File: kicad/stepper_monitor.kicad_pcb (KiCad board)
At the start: 2 copper layers, 53 parts, among them J1 USB_C_Receptacle_USB2.0, J2 Conn_01x02_Male, J3 JTAG, J4 Conn_01x04_Male, J5 Conn_01x04_Male, Q1 UMH3N, Q2 PJA3439, Q3 AO3416, SW1 SW_Push, U1 CP2102N-A01-GQFN28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

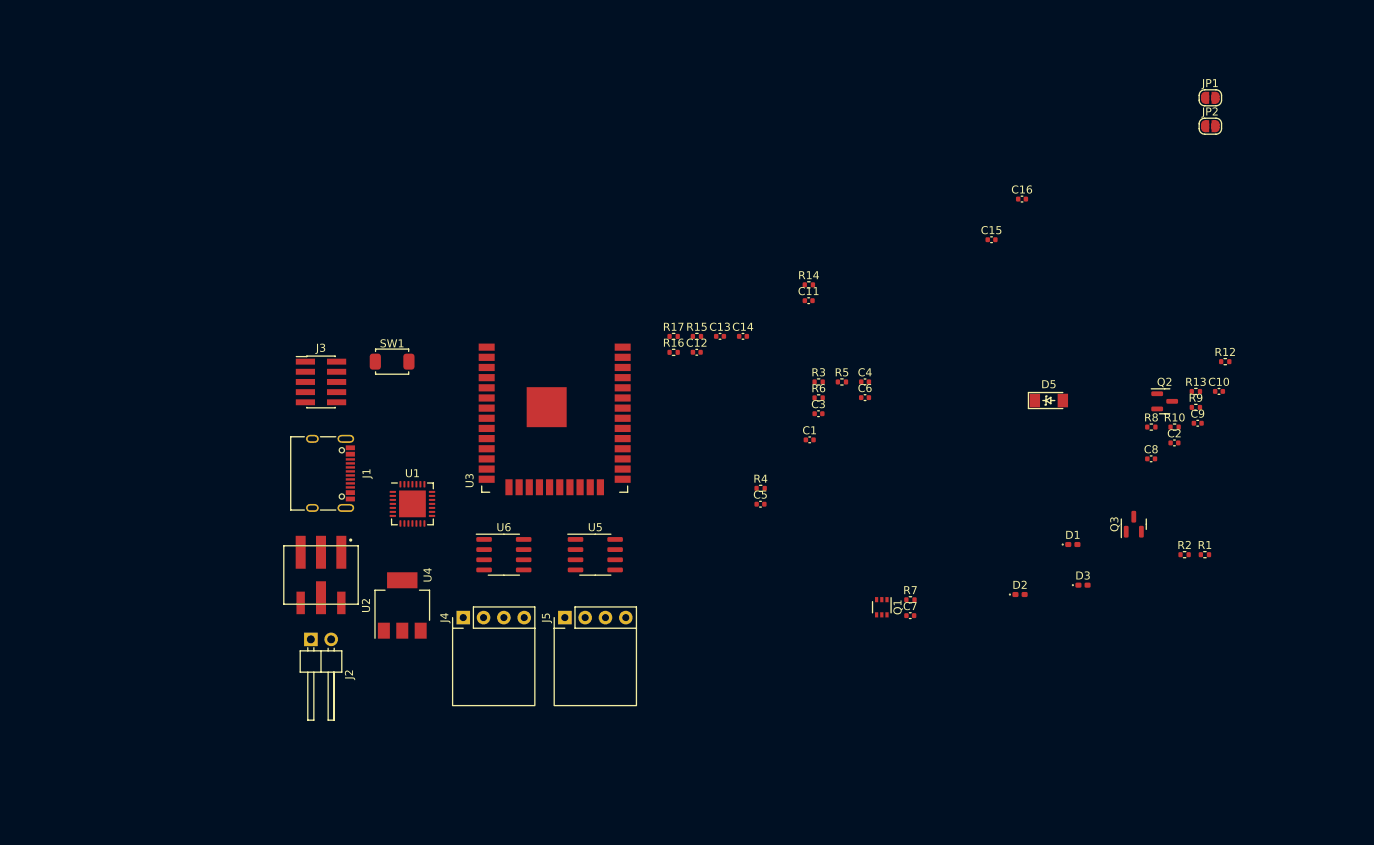
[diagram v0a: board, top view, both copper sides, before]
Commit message: Cleaned up a few footprints.
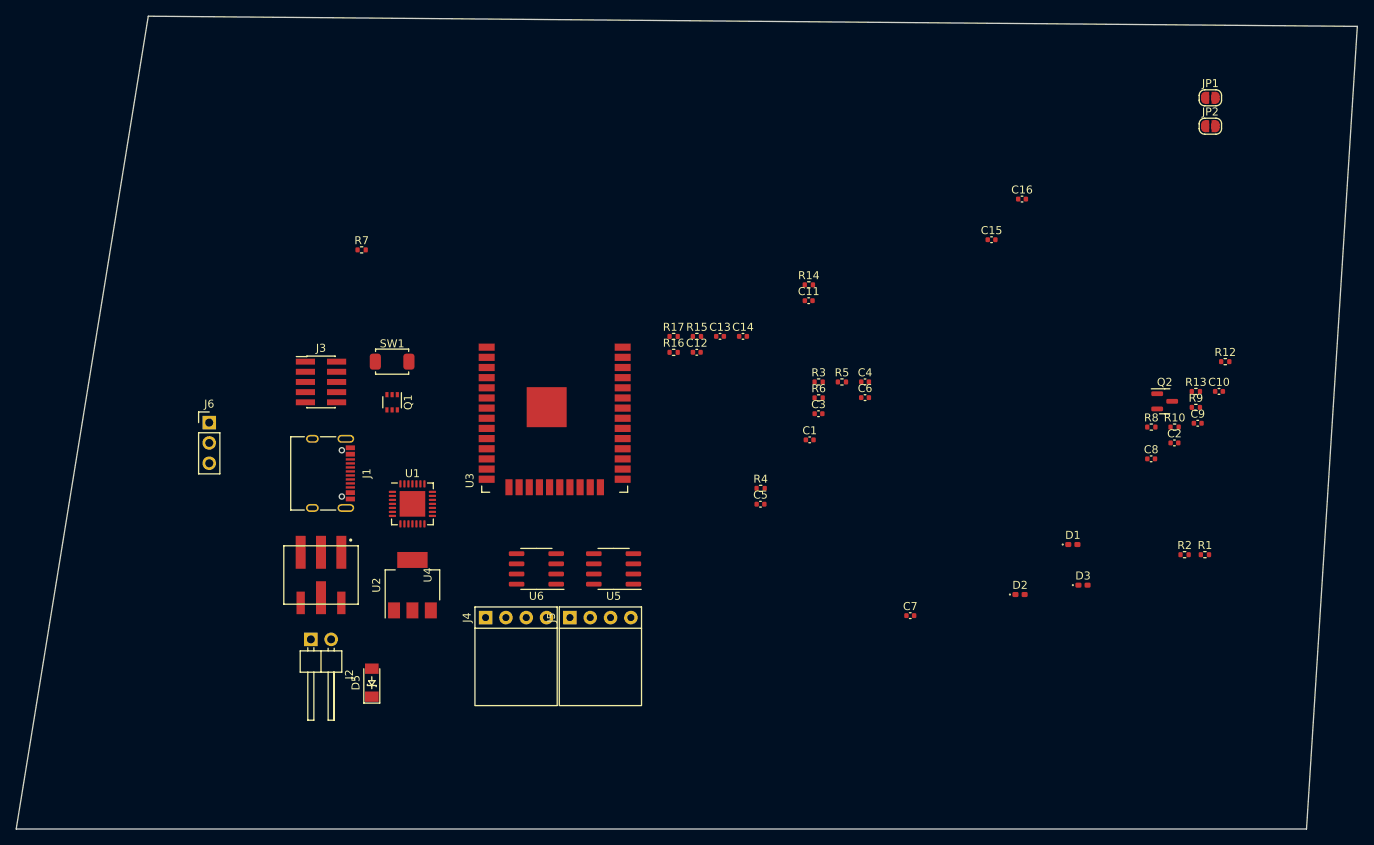
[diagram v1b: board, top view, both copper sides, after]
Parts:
- removed Q3: AO3416, Package_TO_SOT_SMD:SOT-23
- added J6: Conn_01x03_Male, Connector_PinHeader_2.54mm:PinHeader_1x03_P2.54mm_Vertical, F.Cu at (55.9, 77.5)
- U1: footprint Package_DFN_QFN:QFN-28-1EP_5x5mm_P0.5mm_EP3.35x3.35mm -> stepper_monitor:QFN-28-1EP_5x5mm_P0.5mm_EP3.35x3.35mm
- moved D5 91.7 mm to (76.2, 110.0), turned to 90 degrees
- moved R7 81.4 mm to (74.9, 55.9)
- moved Q1 66.4 mm to (78.7, 74.9)
- moved U6 4.44 mm to (96.8, 95.8), turned to 180 degrees
- moved U5 2.90 mm to (106.4, 95.8), turned to 180 degrees
- moved U2 2.84 mm to (81.3, 97.8)
- moved J4 2.79 mm to (94.2, 101.8)
- moved J5 0.64 mm to (104.8, 101.8)
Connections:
- C10 pad 2: Net-(C1-Pad2) -> Net-(C10-Pad2)
- C9 pad 2: Net-(C1-Pad2) -> Net-(C10-Pad2)
- U4 pad 3: Net-(C1-Pad2) -> Net-(C10-Pad2)
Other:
- board outline added: 167.6 x 101.6 mm

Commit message: Initial placement and routing. Needs TLC.
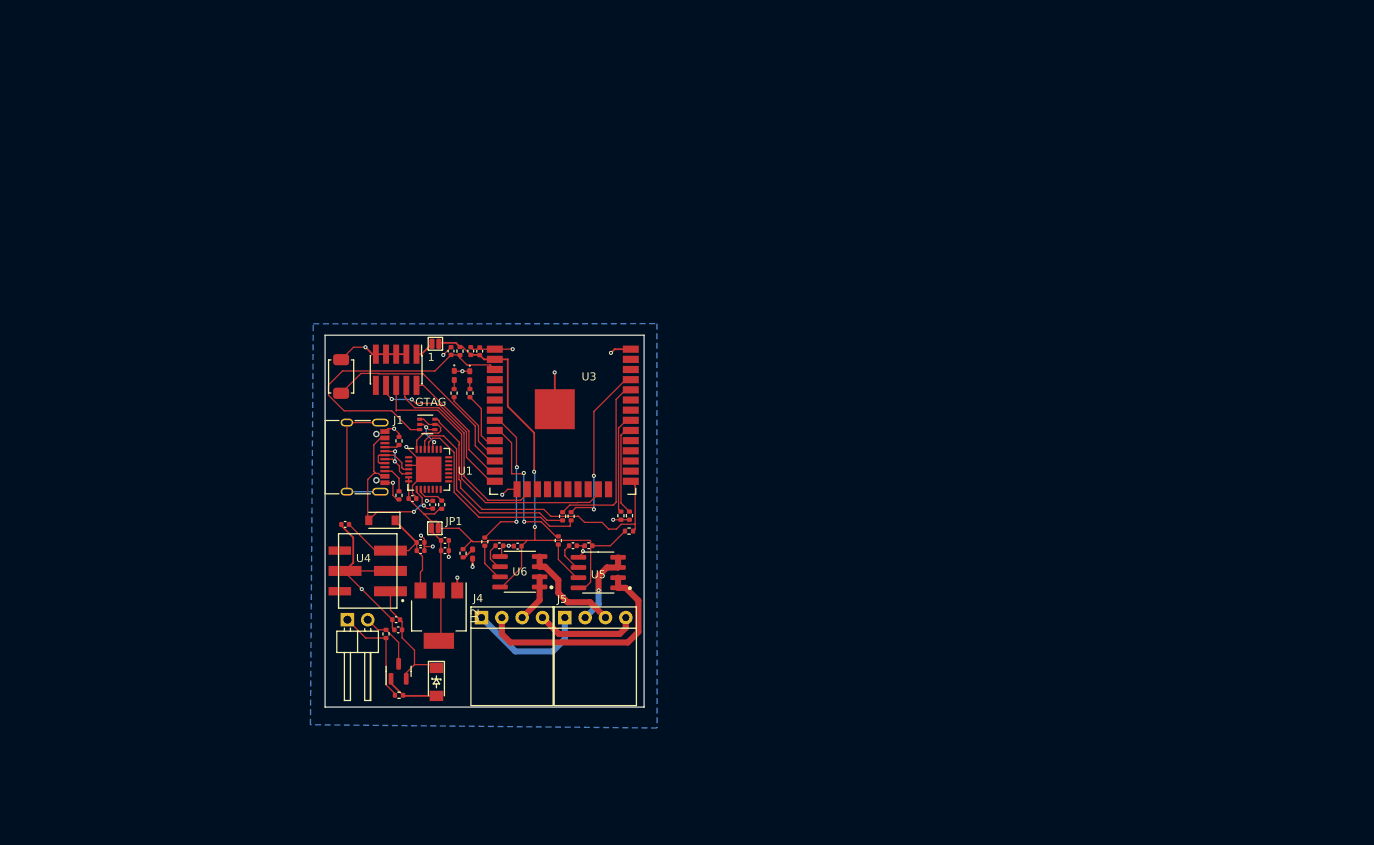
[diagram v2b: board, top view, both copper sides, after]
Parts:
- removed J6: Conn_01x03_Male, Connector_PinHeader_2.54mm:PinHeader_1x03_P2.54mm_Vertical
- added D4: D_Schottky, Diode_SMD:D_SOD-123, F.Cu at (77.5, 89.7)
- JP1, JP2: footprint Jumper:SolderJumper-2_P1.3mm_Open_RoundedPad1.0x1.5mm -> stepper_monitor:SolderJumper-2_P1.3mm_Open_RoundedPad1.0x1.5mm
- U5, U6: footprint Package_SO:SOIC-8_3.9x4.9mm_P1.27mm -> stepper_monitor:SOIC-8_3.9x4.9mm_P1.27mm
- moved JP1 110.9 mm to (84.1, 90.7)
- moved R12 110.3 mm to (78.0, 103.9), turned to -90 degrees
- moved C9 107.3 mm to (72.9, 90.2)
- moved R13 106.6 mm to (79.6, 111.6), turned to 180 degrees
- moved C10 101.8 mm to (82.3, 93.5), turned to 180 degrees
- moved R1 101.7 mm to (79.6, 79.8), turned to -90 degrees
- moved Q2 101.5 mm to (79.6, 108.6), turned to 90 degrees
- moved JP2 100.6 mm to (84.2, 67.6), turned to 180 degrees
- moved C2 99.8 mm to (79.2, 102.1)
- moved R2 98.5 mm to (79.6, 86.6), turned to 90 degrees
- moved C8 96.5 mm to (79.5, 103.4)
- moved R9 80.3 mm to (100.1, 89.2), turned to -90 degrees
- moved D1 80.2 mm to (86.5, 71.6), turned to -90 degrees
- moved D3 76.4 mm to (88.8, 93.9), turned to 90 degrees
- moved D2 74.0 mm to (88.4, 71.6), turned to -90 degrees
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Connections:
- C10 pad 2: Net-(C10-Pad2) -> Net-(C1-Pad2)
- C9 pad 2: Net-(C10-Pad2) -> Net-(C1-Pad2)
- Q1 pad 1: RTS -> DTR
- Q1 pad 2: DTR -> RTS
- Q1 pad 3: IO0 -> EN
- Q1 pad 4: DTR -> RTS
- Q1 pad 5: RTS -> DTR
- Q1 pad 6: EN -> IO0
- U3 pad 10: SWITCH -> LED2
- U3 pad 12: LED2 -> SWITCH
- U4 pad 3: Net-(C10-Pad2) -> Net-(C1-Pad2)
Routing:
- net GNDD: track 0.00 -> 97.4 mm, vias 0 -> 20
- net +3V3: track 0.00 -> 85.1 mm, vias 0 -> 2
- net IO0: track 0.00 -> 40.9 mm
- net EN: track 0.00 -> 37.8 mm
- net ESP_TDO: track 0.00 -> 37.6 mm
- net Net-(J4-Pad2): track 0.00 -> 28.5 mm
- net Net-(R8-Pad2): track 0.00 -> 27.0 mm
- net ESP_TCK: track 0.00 -> 26.3 mm
- net SWITCH: track 0.00 -> 26.2 mm
- net Net-(R9-Pad2): track 0.00 -> 25.9 mm
- net VBUS: track 0.00 -> 24.5 mm, vias 0 -> 2
- net RXD0: track 0.00 -> 22.4 mm
- net TXD0: track 0.00 -> 21.7 mm, vias 0 -> 2
- net ESP_TDI: track 0.00 -> 21.0 mm, vias 0 -> 2
- net Net-(C1-Pad2): track 0.00 -> 20.5 mm
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- added copper zone on B.Cu, net GNDD
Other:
- board size 167.6 x 101.6 mm -> 39.9 x 46.5 mm
- board text added: "1"
- board text added: "GTAG"

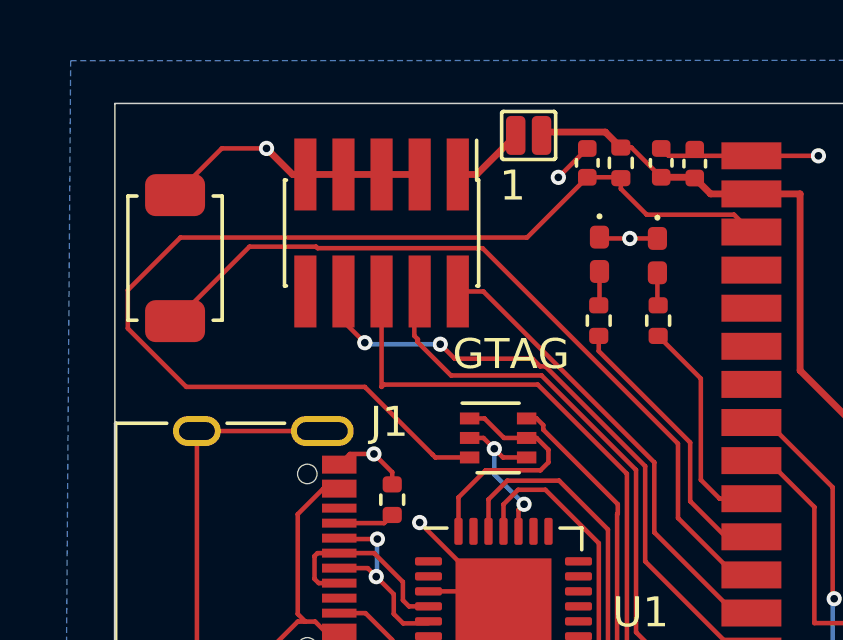
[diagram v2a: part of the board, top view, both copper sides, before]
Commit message: Fixed non available JLCPCB parts.
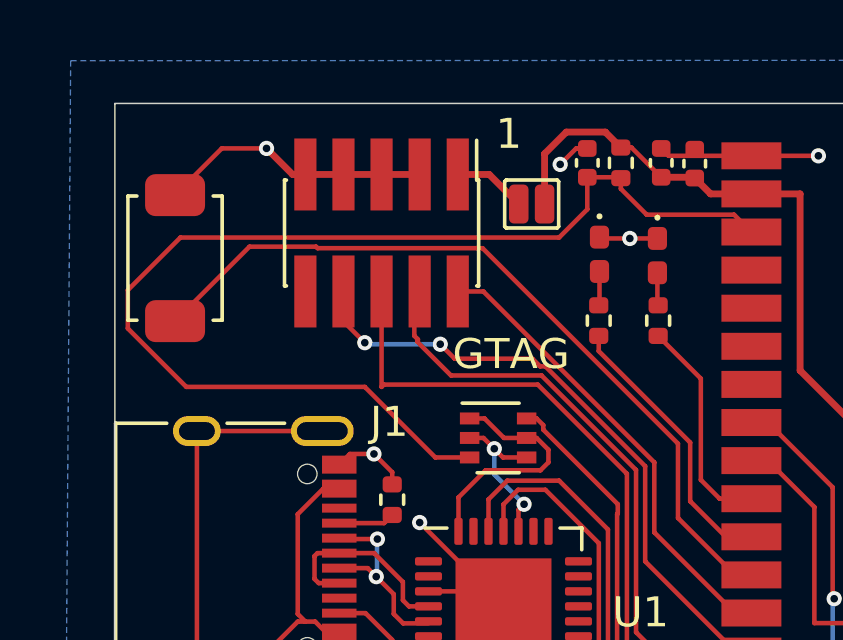
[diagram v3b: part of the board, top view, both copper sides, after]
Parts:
- U3: value ESP32-WROOM-32D -> ESP32-WROOM-32
- moved JP2 2.29 mm to (84.3, 69.9)
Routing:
- net +3V3: track 85.1 -> 86.9 mm
- net EN: track 37.8 -> 38.4 mm

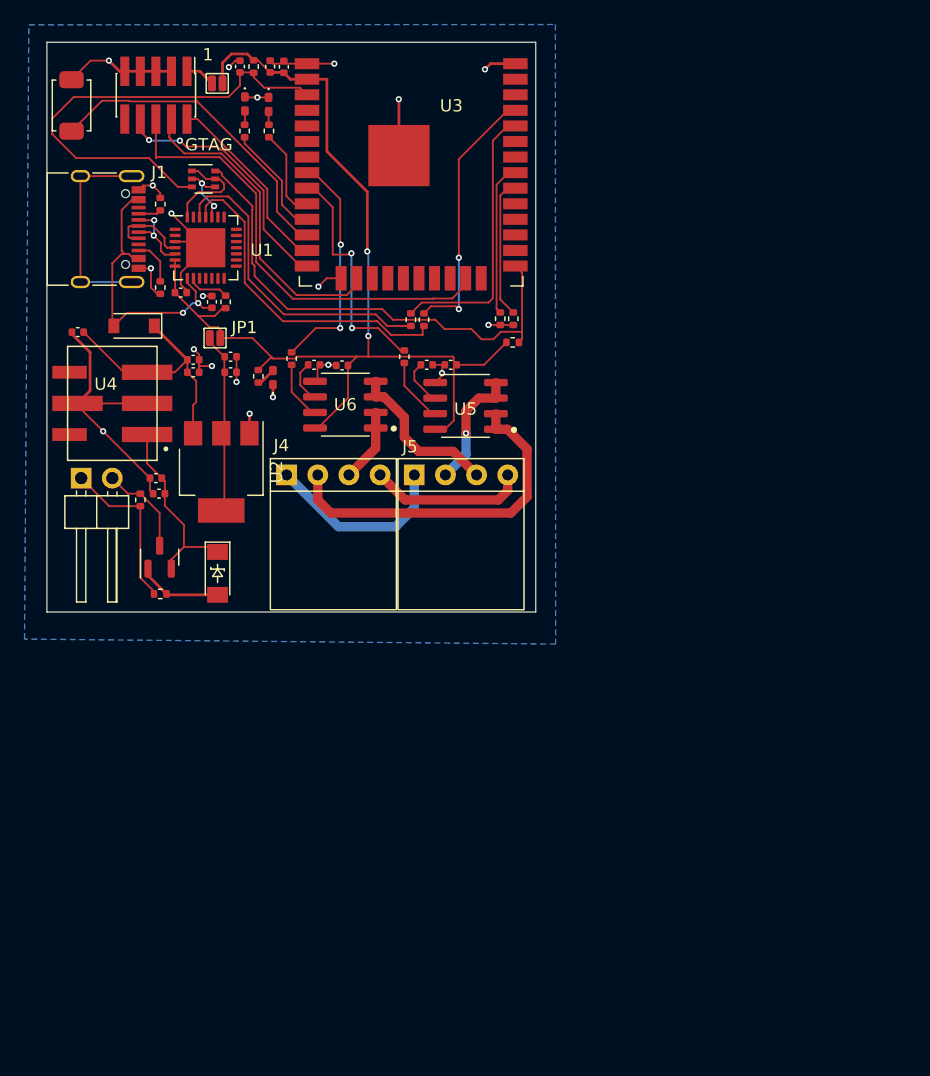
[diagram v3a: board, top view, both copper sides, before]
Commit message: Topologically correct routing. Needs TLC.
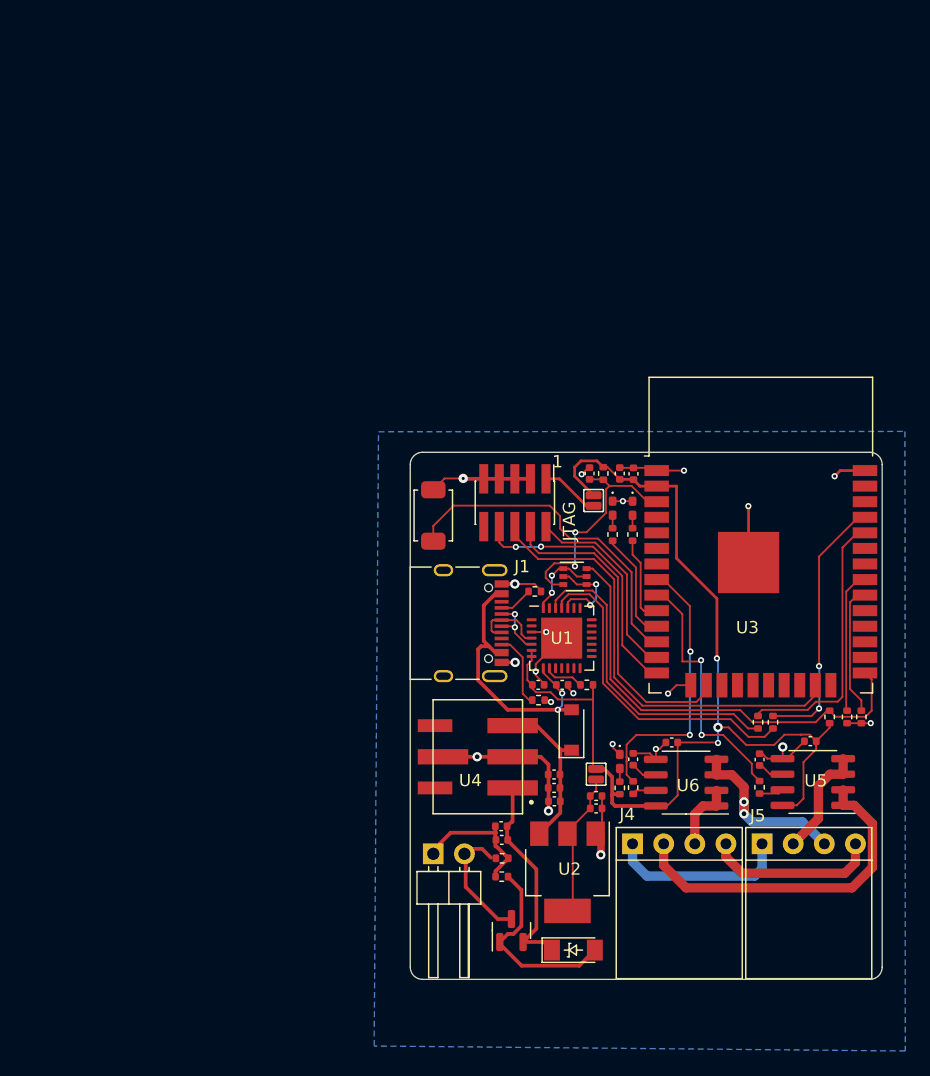
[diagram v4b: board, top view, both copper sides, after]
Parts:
- D5: footprint stepper_probe:D_MiniMELF_zenner -> stepper_monitor:D_MiniMELF_zenner
- U1: footprint stepper_monitor:QFN-28-1EP_5x5mm_P0.5mm_EP3.35x3.35mm -> Package_DFN_QFN:QFN-28-1EP_5x5mm_P0.5mm_EP3.35x3.35mm
- U2: footprint Package_TO_SOT_SMD:SOT-223-3_TabPin2 -> stepper_monitor:SOT-223-3_TabPin2
- U3: footprint stepper_monitor:ESP32-WROOM-32 -> RF_Module:ESP32-WROOM-32
- U5, U6: footprint stepper_monitor:SOIC-8_3.9x4.9mm_P1.27mm -> Package_SO:SOIC-8_3.9x4.9mm_P1.27mm
- moved C9 54.6 mm to (111.8, 128.5)
- moved D4 48.6 mm to (113.2, 122.7), turned to 90 degrees
- moved JP1 47.3 mm to (115.2, 126.3), turned to 90 degrees
- moved C4 46.6 mm to (115.2, 128.0)
- moved C3 46.4 mm to (115.2, 129.1)
- moved JP2 45.8 mm to (115.0, 103.9), turned to -90 degrees
- moved C1 45.7 mm to (111.7, 127.4), turned to 0 degrees
- moved R2 45.7 mm to (110.5, 120.2), turned to 180 degrees
- moved R14 45.5 mm to (128.5, 127.3)
- moved R15 44.7 mm to (118.2, 127.4)
- moved R3 44.7 mm to (117.1, 127.4), turned to -90 degrees
- moved SW1 44.6 mm to (101.9, 105.2)
- moved D1 44.6 mm to (116.5, 104.6)
- moved R4 44.6 mm to (116.5, 106.7)
- moved Q1 44.4 mm to (113.4, 110.1)
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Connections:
- J1 pad S1: unconnected-(J1-PadS1) -> (no net)
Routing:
- net EN: track 38.4 -> 19.4 mm, vias 0 -> 2
- net GNDD: track 97.2 -> 80.0 mm
- net unconnected-(J1-PadS1): track 17.0 -> 0.00 mm
- net Net-(D5-Pad2): track 6.88 -> 16.0 mm
- net Net-(C1-Pad2): track 20.5 -> 12.9 mm
- net CHA: track 18.9 -> 22.9 mm
- net IO0: track 40.9 -> 37.0 mm
- net Net-(C3-Pad2): track 14.7 -> 11.3 mm
- net Net-(R14-Pad2): track 5.32 -> 2.00 mm
- net Net-(R15-Pad2): track 4.82 -> 1.96 mm
- net Net-(J2-Pad2): track 7.71 -> 10.3 mm
- net Net-(J3-Pad1): track 2.44 -> 4.80 mm
- net Net-(J1-PadB5): track 3.76 -> 5.89 mm
- net RTS: track 5.41 -> 7.52 mm
- net DTR: track 8.09 -> 6.23 mm, vias 0 -> 2
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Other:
- board size 39.9 x 46.5 mm -> 38.5 x 43 mm
- board text added: "JTAG"
- board text removed: "GTAG"

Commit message: Cleaned up the layout.
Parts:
- removed JP2: SolderJumper_2_Open, stepper_monitor:SolderJumper-2_P1.3mm_Open_RoundedPad1.0x1.5mm
- D4: footprint Diode_SMD:D_SOD-123 -> stepper_monitor:D_SOD-123
- Q1: footprint Package_TO_SOT_SMD:SOT-363_SC-70-6 -> stepper_monitor:SOT-363_SC-70-6
- U1: footprint Package_DFN_QFN:QFN-28-1EP_5x5mm_P0.5mm_EP3.35x3.35mm -> stepper_monitor:QFN-28-1EP_5x5mm_P0.5mm_EP3.35x3.35mm
- U3: footprint RF_Module:ESP32-WROOM-32 -> stepper_monitor:ESP32-WROOM-32
- U5, U6: footprint Package_SO:SOIC-8_3.9x4.9mm_P1.27mm -> stepper_monitor:SOIC-8_3.9x4.9mm_P1.27mm
- moved D5 0.75 mm to (112.9, 140.0)
- moved Q2 0.60 mm to (108.0, 138.5)
- turned R13 to 0 degrees
- renumbered J4 to J1, J5 to J2, J2 to J3, J1 to J4, J3 to J5
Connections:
- J5 pad 1: Net-(J3-Pad1) -> unconnected-(J5-Pad1)
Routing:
- net Net-(J3-Pad1): track 4.80 -> 0.00 mm
- net GNDD: track 80.0 -> 75.6 mm, vias 20 -> 22
- net +3V3: track 86.4 -> 88.3 mm
- net Net-(J3-Pad2): track 10.3 -> 9.68 mm
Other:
- board text added: "+"
- board text added: "7-30VDC"
- board text added: "STEPPER MOTOR ANALYZER V1.4 ESP32 OSH, github/zapta"
- board text added: "V1.4"
